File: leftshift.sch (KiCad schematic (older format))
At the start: 9 parts

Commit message: Cleaned up left shift
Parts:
- removed LS1: MX-2.25U, symbol MX-2.25U
- removed LS3, LS4: MX-1U, symbol MX-1U
- removed LS5: MX-1.25U, symbol MX-1.25U
- added DLS?: 1N4148WS, symbol D
- added LS1: MX-1U, symbol MX-1U
- added LS3, LS4: MX-1U-FLIPPED, symbol MX-1U-FLIPPED
- added LS5: MX-1.25U-FLIPPED, symbol MX-1.25U-FLIPPED
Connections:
- net leftshift5V: now also RLS1.1, RLS2.1, DLS?.2 (A); no longer LS2.3 (LED), LS6.3 (LED)
- net leftshiftLEDGND: now also LS2.4 (LEDGND), LS1.4 (LEDGND), LS3.4 (LEDGND), LS5.4 (LEDGND); no longer RLS1.2, RLS2.2
- net leftshiftcol1: now also DLS1.2 (A); no longer LS2.1 (COL)
- net leftshiftrow1: now also LS2.2 (ROW), LS6.2 (ROW), LS1.2 (ROW), LS3.1 (ROW), LS4.1 (ROW), LS5.1 (ROW); no longer DLS1.1 (K)
- net at LS6.4 (LEDGND): now also LS4.4 (LEDGND); no longer RLS2.1
- net leftshiftcol2: no longer names the net of LS6.1 (COL)
- net leftshiftcol2: now also DLS?.1 (K), LS4.2 (COL)
- new net: DLS1.1 (K), LS1.1 (COL), LS2.1 (COL), LS3.2 (COL), LS5.2 (COL)
- new net: LS1.3 (LED), LS2.3 (LED), LS3.3 (LED), LS5.3 (LED), RLS1.2
- new net: LS4.3 (LED), LS6.3 (LED), RLS2.2
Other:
- moved on the sheet: DLS1, RLS1, RLS2

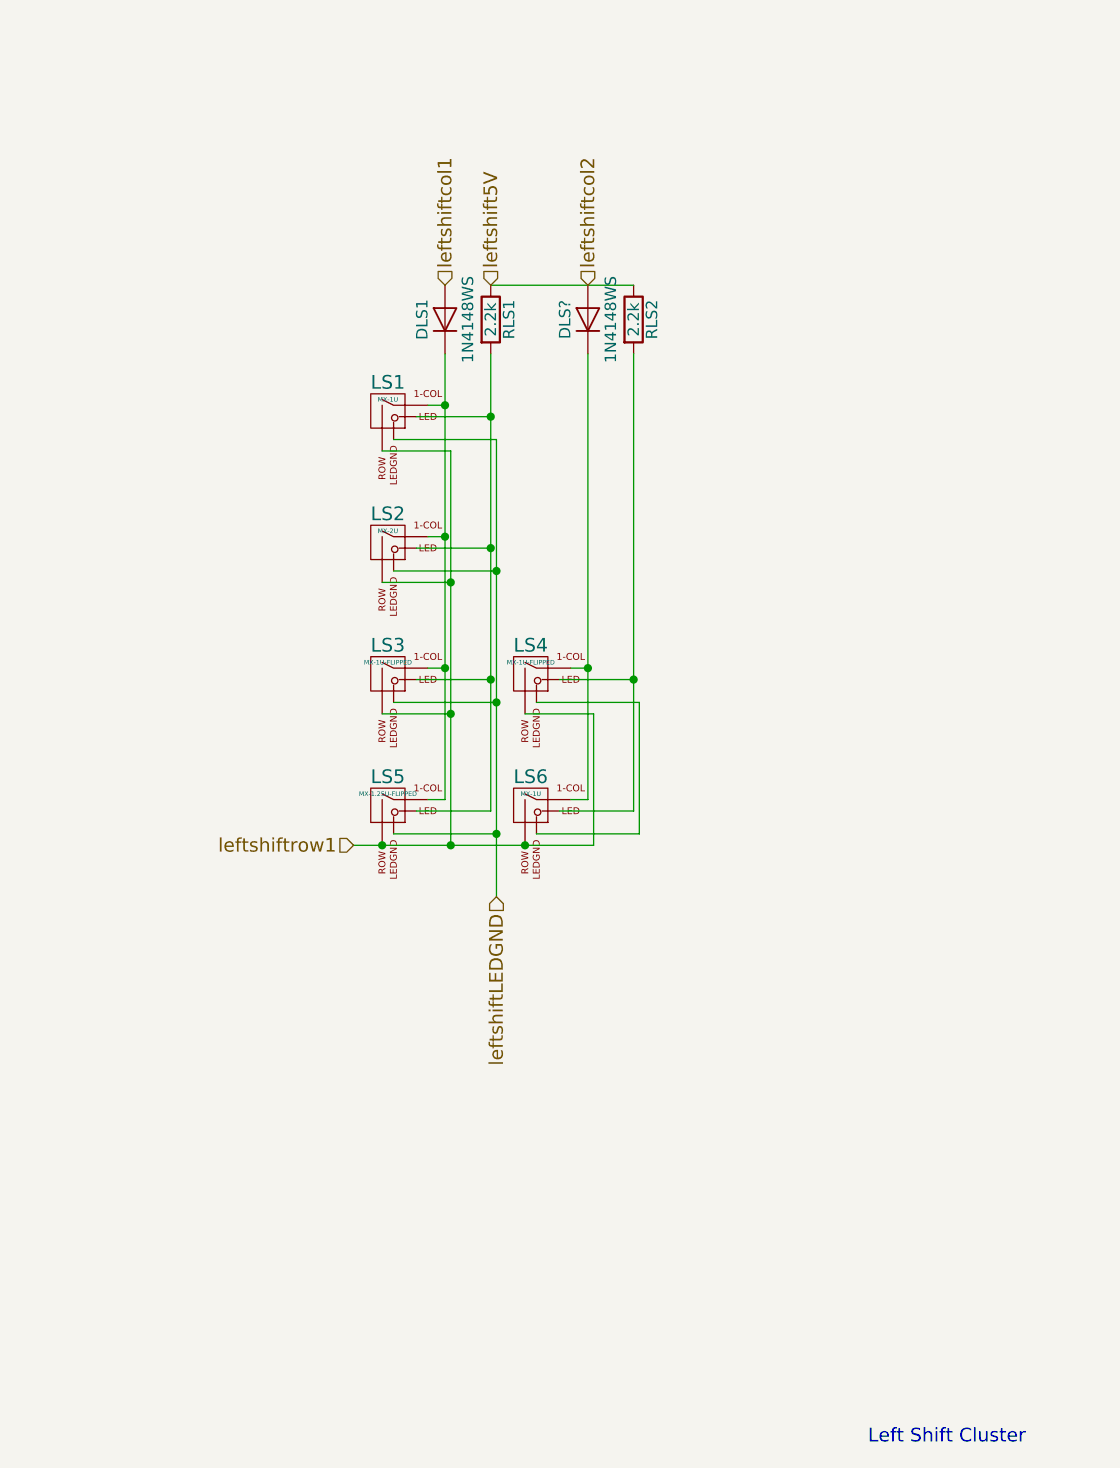
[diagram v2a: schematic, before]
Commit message: Added spacebar schematic
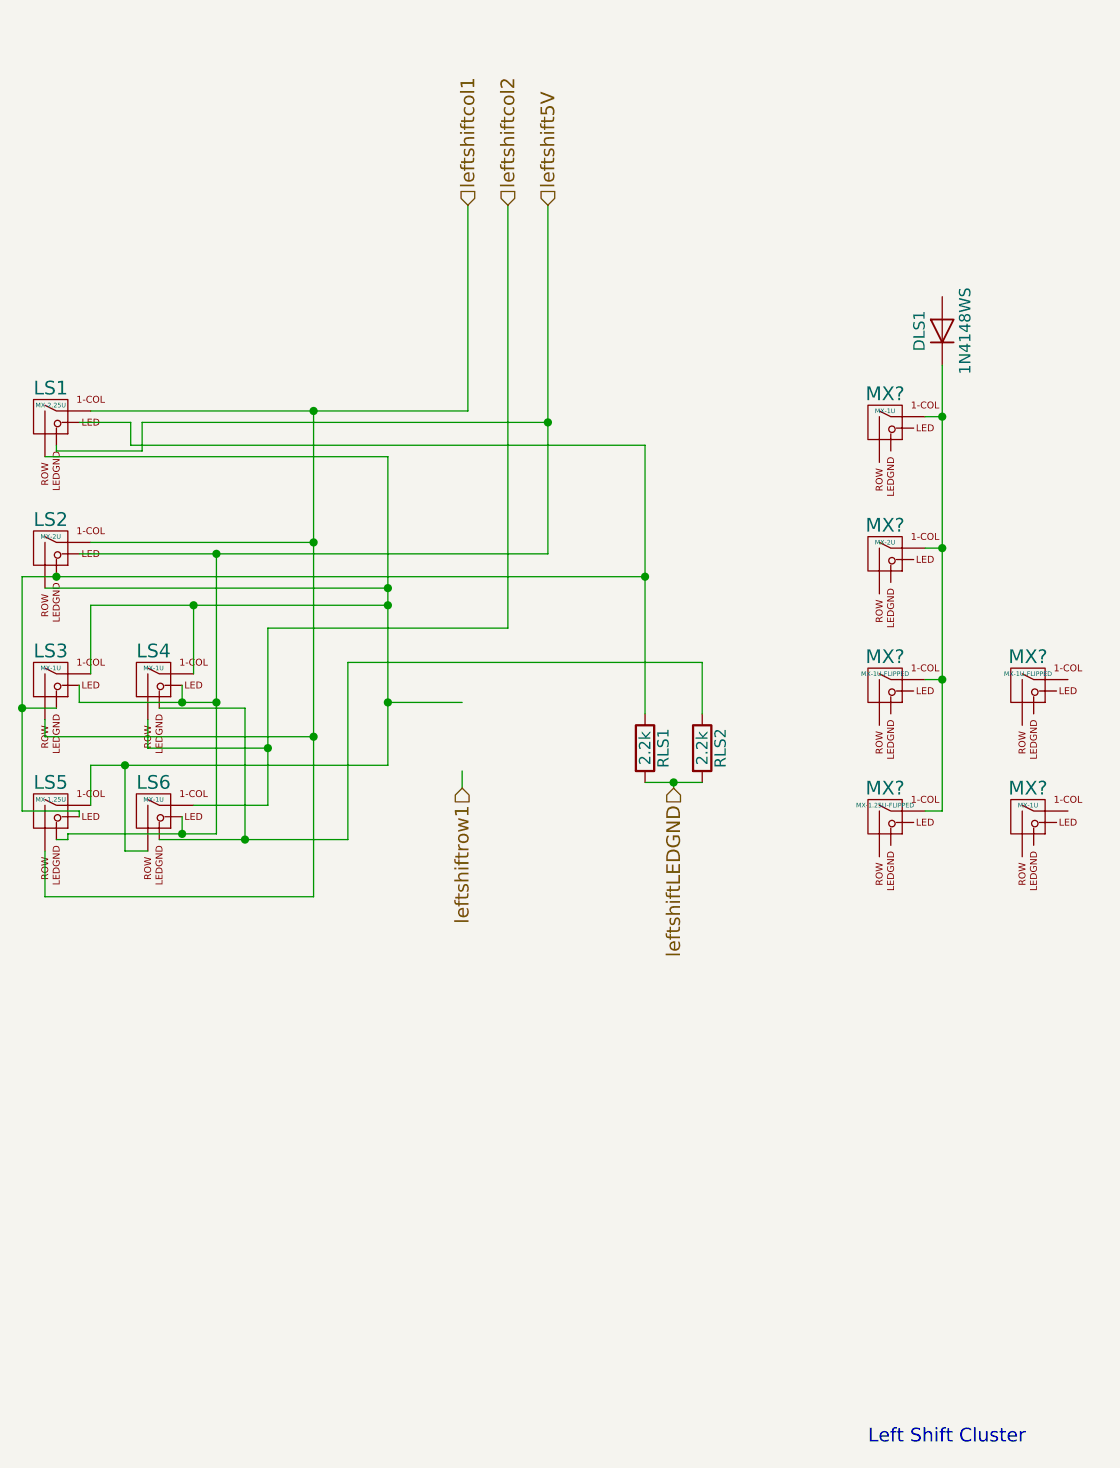
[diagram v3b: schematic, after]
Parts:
- removed DLS?: 1N4148WS, symbol D
- added LS1: MX-2.25U, symbol MX-2.25U
- added LS2: MX-2U, symbol MX-2U
- added LS3, LS4, LS6: MX-1U, symbol MX-1U
- added LS5: MX-1.25U, symbol MX-1.25U
- renumbered LS1 to MX?, LS2 to MX?, LS3 to MX?, LS4 to MX?, LS5 to MX?, LS6 to MX?
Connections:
- wire segments 32 -> 62
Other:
- moved on the sheet: DLS1, MX?, RLS1, RLS2

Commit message: Clean up left shift
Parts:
- removed LS1: MX-2.25U, symbol MX-2.25U
- removed LS2: MX-2U, symbol MX-2U
- removed LS3, LS4, LS6: MX-1U, symbol MX-1U
- removed LS5: MX-1.25U, symbol MX-1.25U
- added DLS2: 1N4148WS, symbol D
- gave numbers to parts that had none: 6
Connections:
- wire segments 62 -> 35
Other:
- moved on the sheet: DLS1, LS1, LS2, LS3, LS4, LS5, LS6, RLS1, RLS2

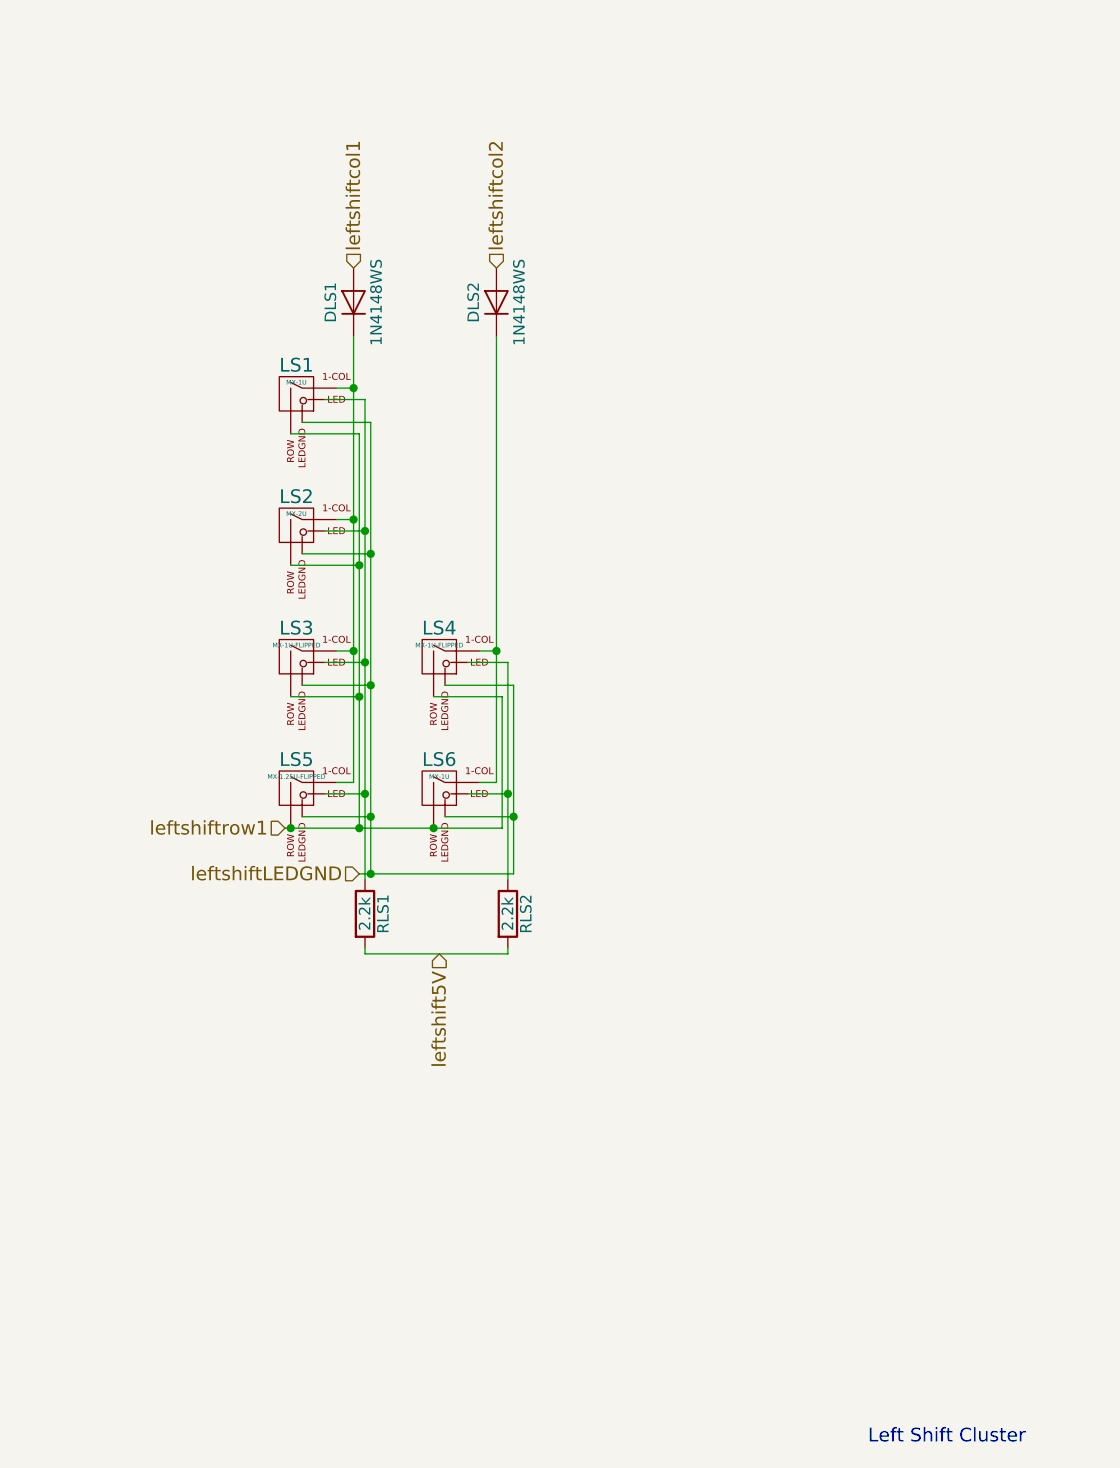
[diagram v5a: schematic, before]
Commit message: Updated component labels
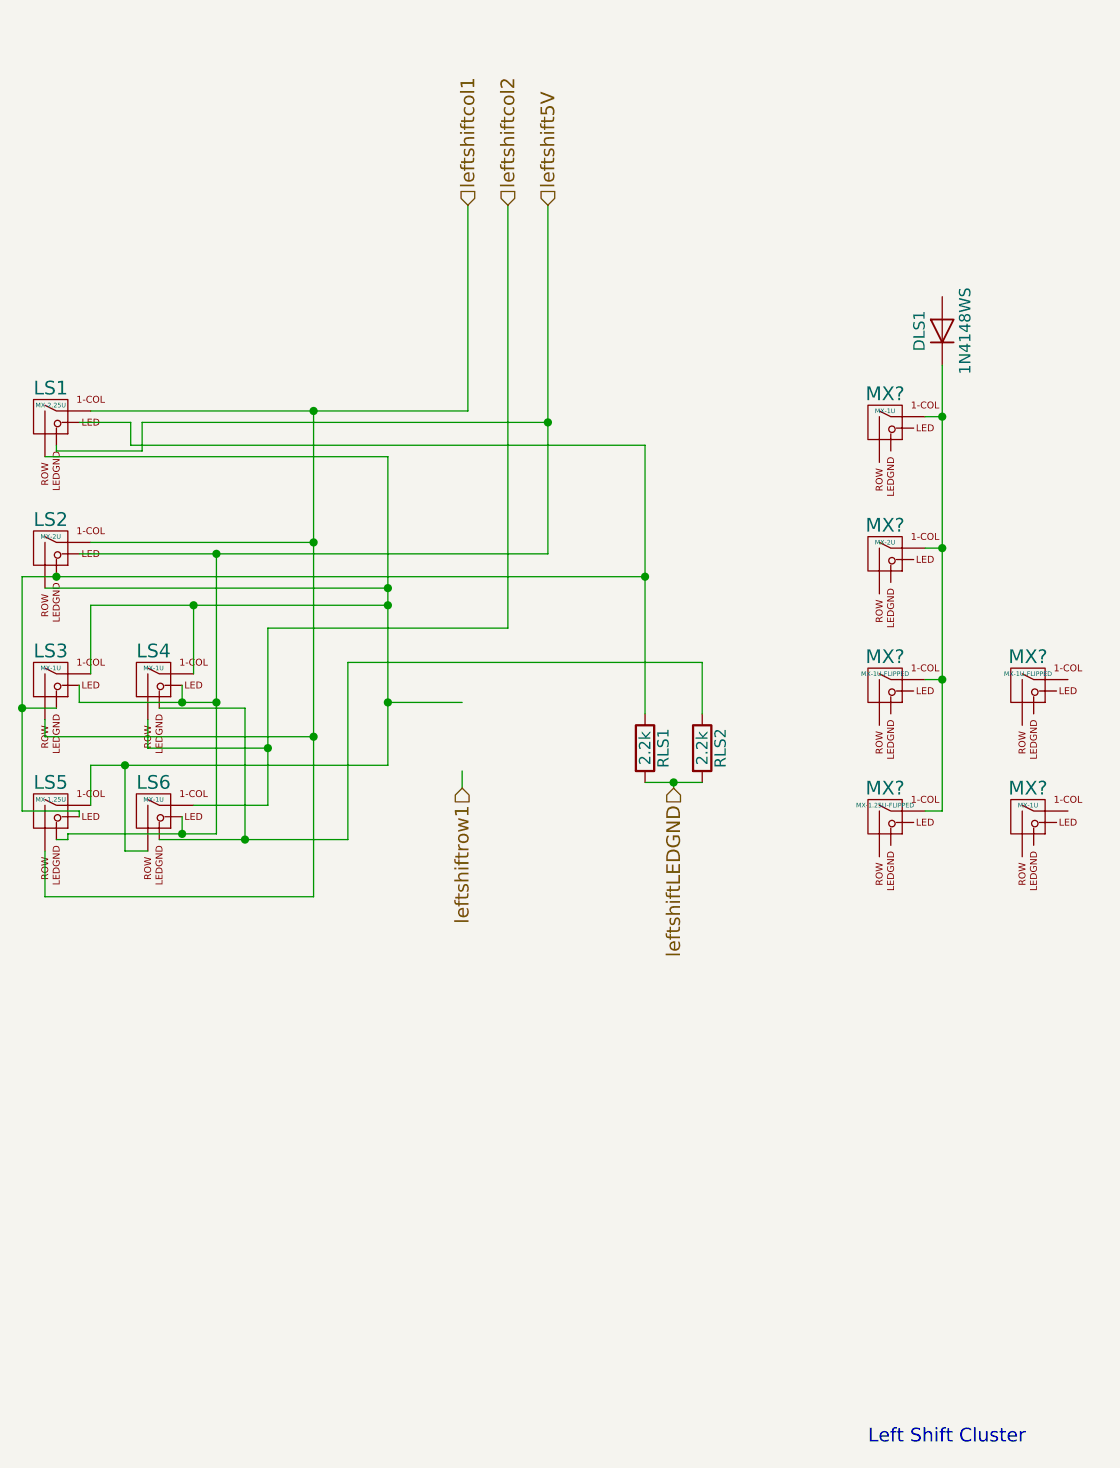
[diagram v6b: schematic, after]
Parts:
- removed DLS2: 1N4148WS, symbol D
- added LS1: MX-2.25U, symbol MX-2.25U
- added LS2: MX-2U, symbol MX-2U
- added LS3, LS4, LS6: MX-1U, symbol MX-1U
- added LS5: MX-1.25U, symbol MX-1.25U
- renumbered LS1 to MX?, LS2 to MX?, LS3 to MX?, LS4 to MX?, LS5 to MX?, LS6 to MX?
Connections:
- wire segments 35 -> 62
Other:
- moved on the sheet: DLS1, MX?, RLS1, RLS2
